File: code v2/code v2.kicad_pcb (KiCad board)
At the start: 2 copper layers, 39 parts, among them J1 PWR-2_pole_power_connector, Q1 2N7000, Q2 2N7000, Q3 2N7000, Q4 2N7000, SW1 SW_DIP_x08, SW2 SW_DIP_x08, U1 74HC04, U2 74HC04, U3 74HC04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

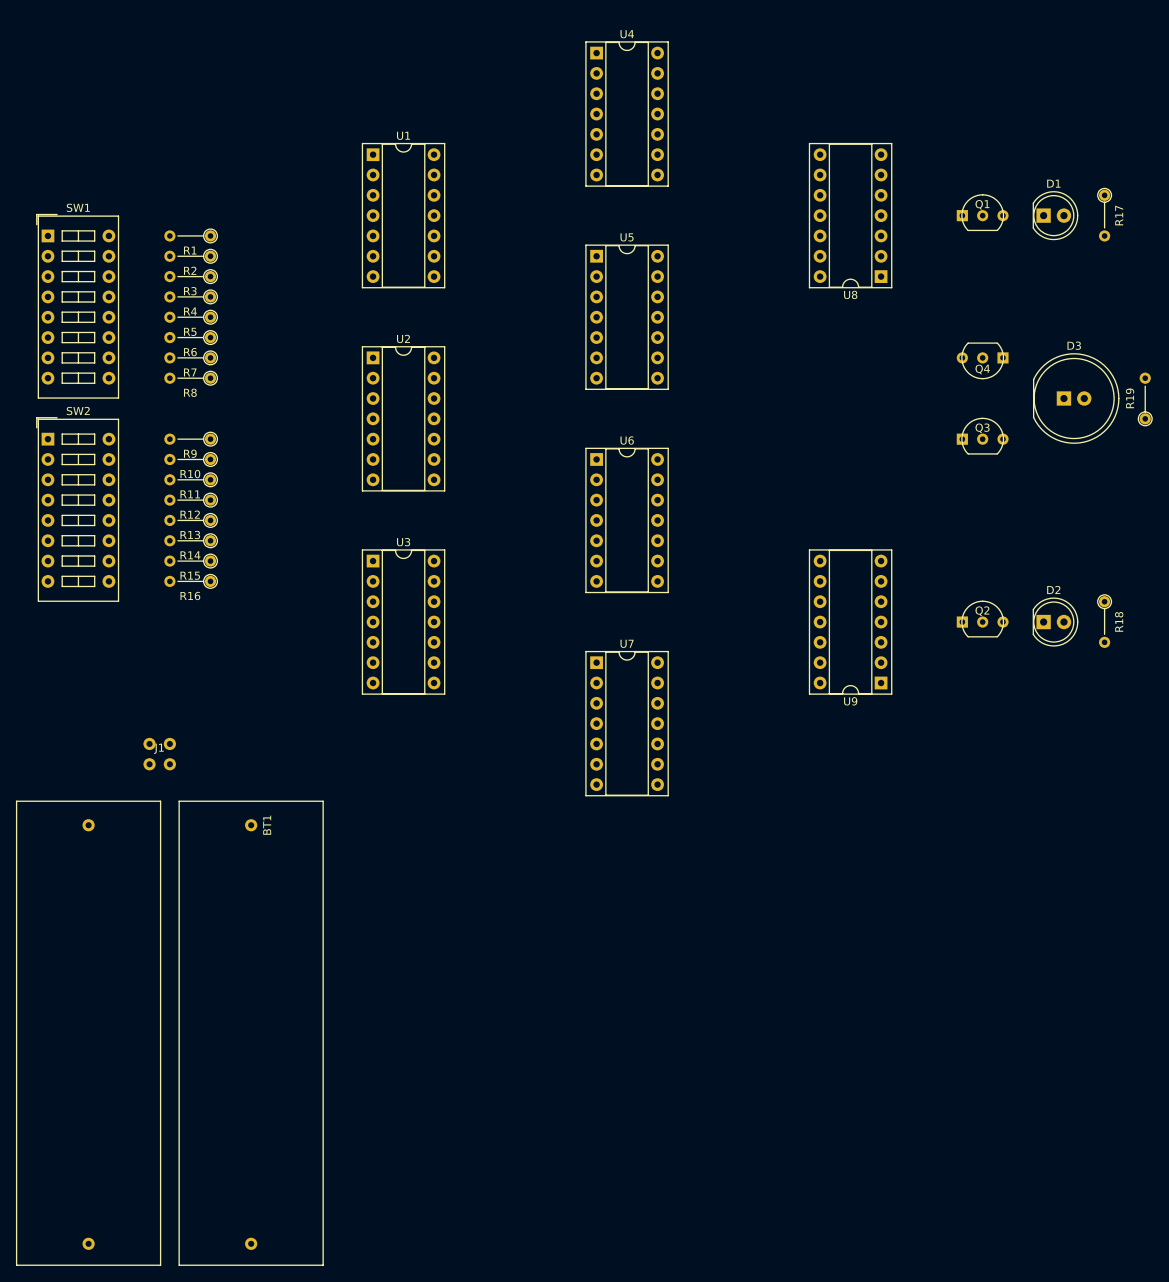
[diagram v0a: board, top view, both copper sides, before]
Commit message: Add finished PCB design
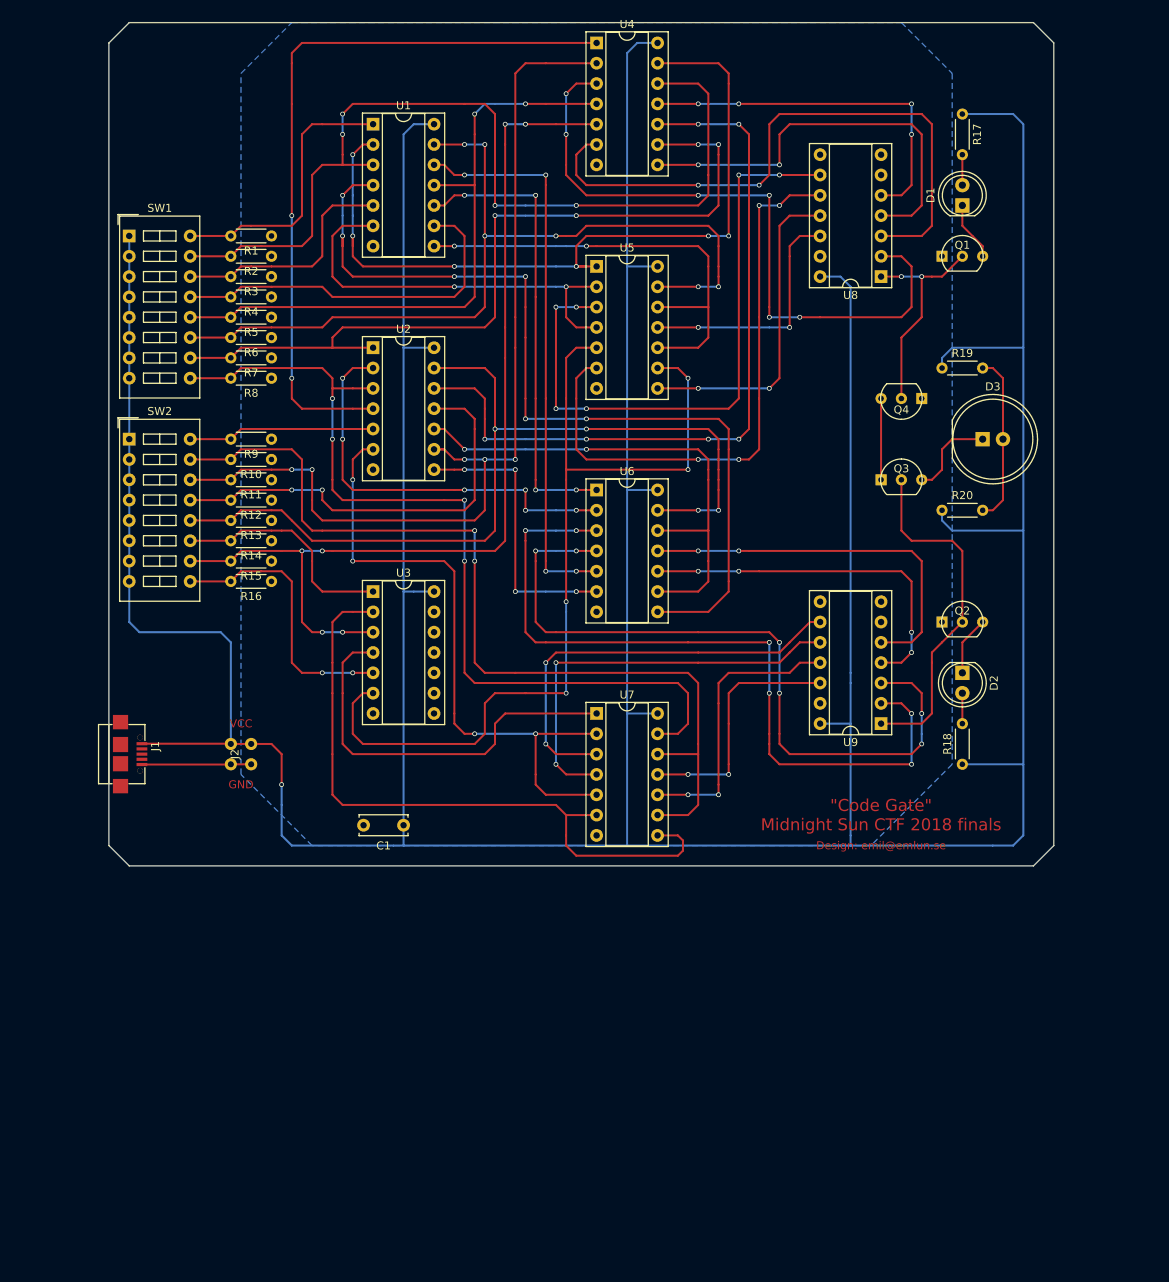
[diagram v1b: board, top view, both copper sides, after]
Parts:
- removed BT1: Battery_Cell, emlun:Battery_holder_2xAA
- added C1: C, Capacitors_THT:C_Disc_D6.0mm_W2.5mm_P5.00mm, F.Cu at (72.4, 137.2)
- added J2: PWR-2_pole_power_connector, emlun:J2x2-double_2_pole_connector, F.Cu at (50.8, 129.5)
- added R20: R, Resistors_THT:R_Axial_DIN0204_L3.6mm_D1.6mm_P5.08mm_Horizontal, F.Cu at (139.7, 97.8)
- J1: value PWR-2_pole_power_connector -> USB_OTG; footprint emlun:J2x2-double_2_pole_connector -> electrokit:USB_Micro-B_Electrokit_anr41011019
- R1, R10, R11, R12, R13, R14, R15, R16, R17, R18, R19, R2, R3, R4, R5, R6, R7, R8, R9: footprint Resistors_THT:R_Axial_DIN0204_L3.6mm_D1.6mm_P5.08mm_Vertical -> Resistors_THT:R_Axial_DIN0204_L3.6mm_D1.6mm_P5.08mm_Horizontal
- U6, U7: value 74HCT02 -> 4001
- moved R18 27.0 mm to (142.2, 129.5), turned to 90 degrees
- moved R19 26.2 mm to (139.7, 80.0), turned to 0 degrees
- moved R17 20.5 mm to (142.2, 48.3)
- moved D2 12.0 mm to (142.2, 118.1), turned to 270 degrees
- moved D3 11.4 mm to (144.8, 88.9)
- moved Q3 11.4 mm to (134.6, 94.0)
- moved Q4 11.4 mm to (134.6, 83.8)
- moved D1 10.2 mm to (142.2, 59.7), turned to 90 degrees
- moved SW1 10.2 mm to (38.1, 63.5)
- moved SW2 10.2 mm to (38.1, 88.9)
- moved R1 7.62 mm to (55.9, 63.5)
- moved R10 7.62 mm to (55.9, 91.4)
- moved R11 7.62 mm to (55.9, 94.0)
- moved R12 7.62 mm to (55.9, 96.5)
- moved R13 7.62 mm to (55.9, 99.1)
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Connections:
- J1 pad 1: GND -> VCC
- J1 pad 2: VCC -> Net-(J1-Pad2)
- U6 pad 1: Net-(U6-Pad1) -> /not_i4
- U6 pad 11: /not_i11 -> Net-(U6-Pad11)
- U6 pad 12: /i12 -> /not_i11
- U6 pad 13: Net-(U6-Pad13) -> /i12
- U6 pad 2: /not_i4 -> /not_i6
- U6 pad 3: /not_i6 -> Net-(U6-Pad3)
- U7 pad 1: Net-(U7-Pad1) -> /not_i14
- U7 pad 11: /i9 -> Net-(U7-Pad11)
- U7 pad 12: /i7 -> /i9
- U7 pad 13: Net-(U7-Pad13) -> /i7
- U7 pad 2: /not_i14 -> /not_i8
- U7 pad 3: /not_i8 -> Net-(U7-Pad3)
- U9 pad 12: Net-(U7-Pad13) -> Net-(U7-Pad11)
- U9 pad 2: Net-(U6-Pad1) -> Net-(U6-Pad3)
- U9 pad 5: Net-(U6-Pad13) -> Net-(U6-Pad11)
- U9 pad 9: Net-(U7-Pad1) -> Net-(U7-Pad3)
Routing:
- net VCC: track 0.00 -> 618.9 mm, vias 0 -> 1
- net /i14: track 0.00 -> 122.2 mm, vias 0 -> 6
- net /i10: track 0.00 -> 120.7 mm, vias 0 -> 5
- net /i1: track 0.00 -> 116.7 mm, vias 0 -> 4
- net /not_i15: track 0.00 -> 116.2 mm, vias 0 -> 4
- net /i9: track 0.00 -> 116.2 mm, vias 0 -> 2
- net /i7: track 0.00 -> 113.6 mm, vias 0 -> 4
- net /i12: track 0.00 -> 112.9 mm, vias 0 -> 4
- net /not_i1: track 0.00 -> 111.9 mm, vias 0 -> 6
- net /i5: track 0.00 -> 109.3 mm, vias 0 -> 6
- net /i6: track 0.00 -> 102.4 mm, vias 0 -> 4
- net /not_i0: track 0.00 -> 101.2 mm, vias 0 -> 6
- net Net-(U6-Pad3): track 0.00 -> 95.6 mm, vias 0 -> 6
- net /not_i12: track 0.00 -> 94.3 mm, vias 0 -> 6
- net /not_i7: track 0.00 -> 92.5 mm, vias 0 -> 2
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- added copper zone on B.Cu, net GND
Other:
- board outline added: 118.1 x 105.4 mm
- board text added: ""Code Gate" Midnight Sun CTF 2018 finals"
- board text added: "Design: emil@emlun.se"
- board text added: "GND"
- board text added: "VCC"

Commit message: Finish some more
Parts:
- moved C1 2.54 mm to (74.9, 137.2)
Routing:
- net GND: track 13.7 -> 517.3 mm
- net VCC: track 618.9 -> 608.0 mm
- removed copper zone on B.Cu, net GND
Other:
- board text removed: "GND"
- board text removed: "VCC"
